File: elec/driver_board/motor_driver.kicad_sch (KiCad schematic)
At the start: 4 parts, among them IC9 TPIC6C595DG4, J9 Connector to the motor board

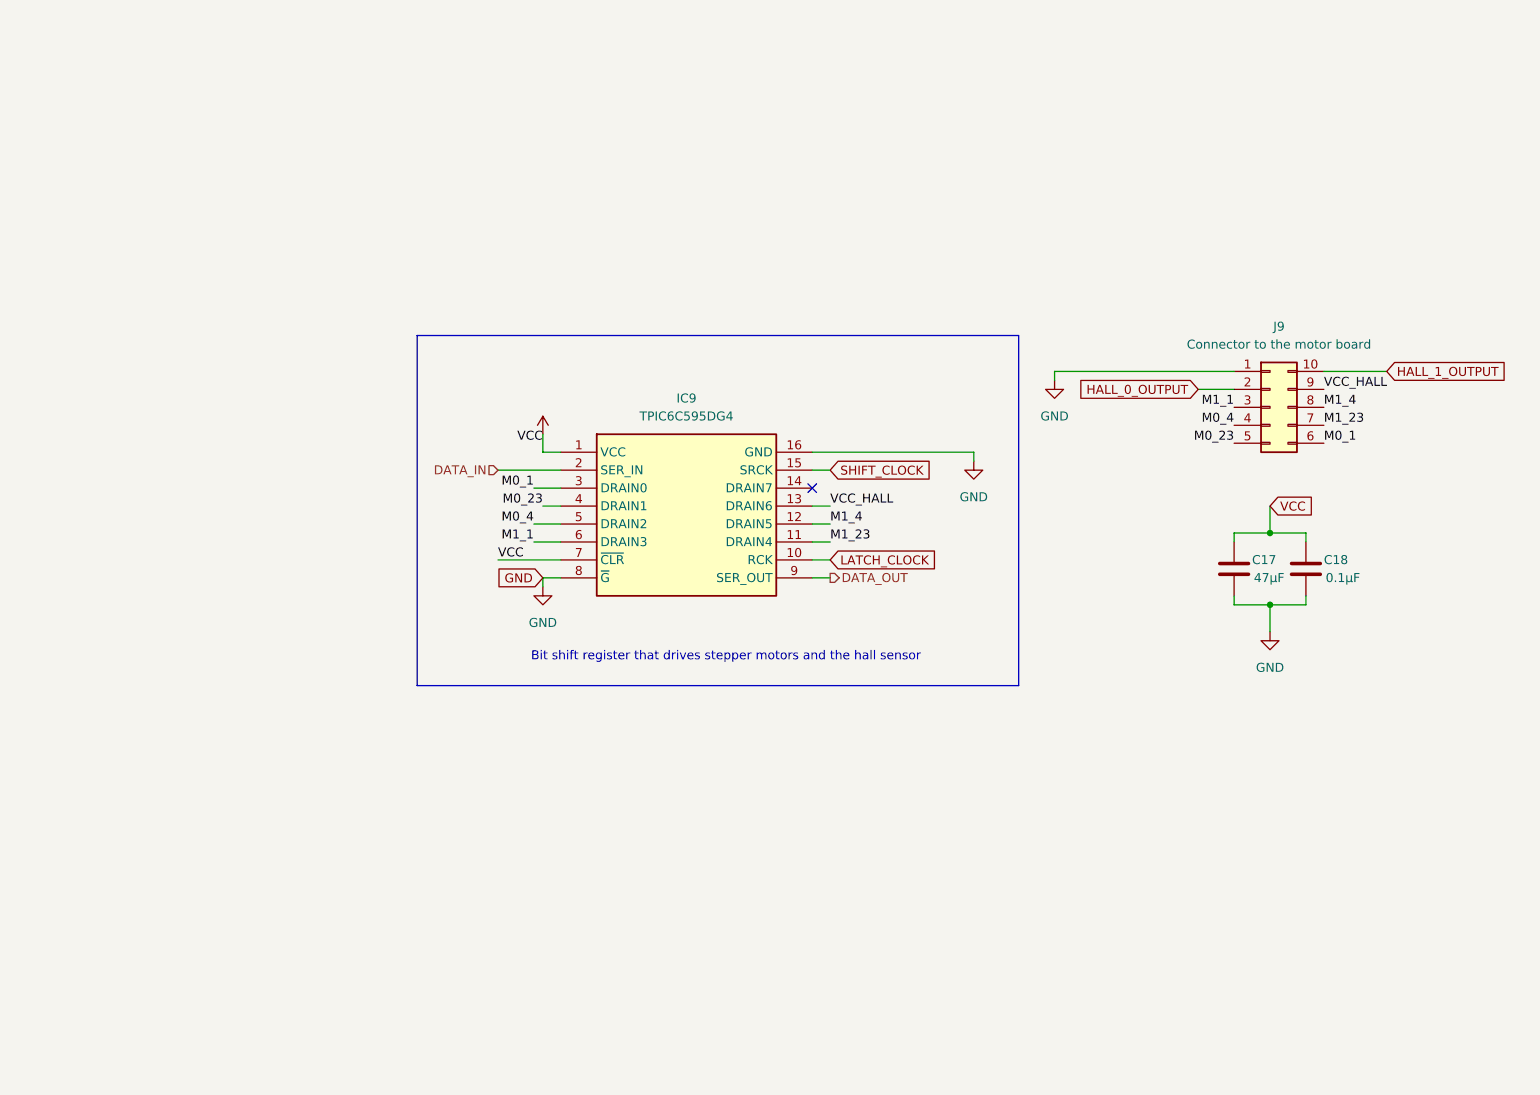
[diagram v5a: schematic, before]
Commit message: Update schematic with VID6606
Use the 'official' driver of VID28-05 motors.
Put back the 74HCT595 bit shift register to link all
motor drivers.
Work in progress.
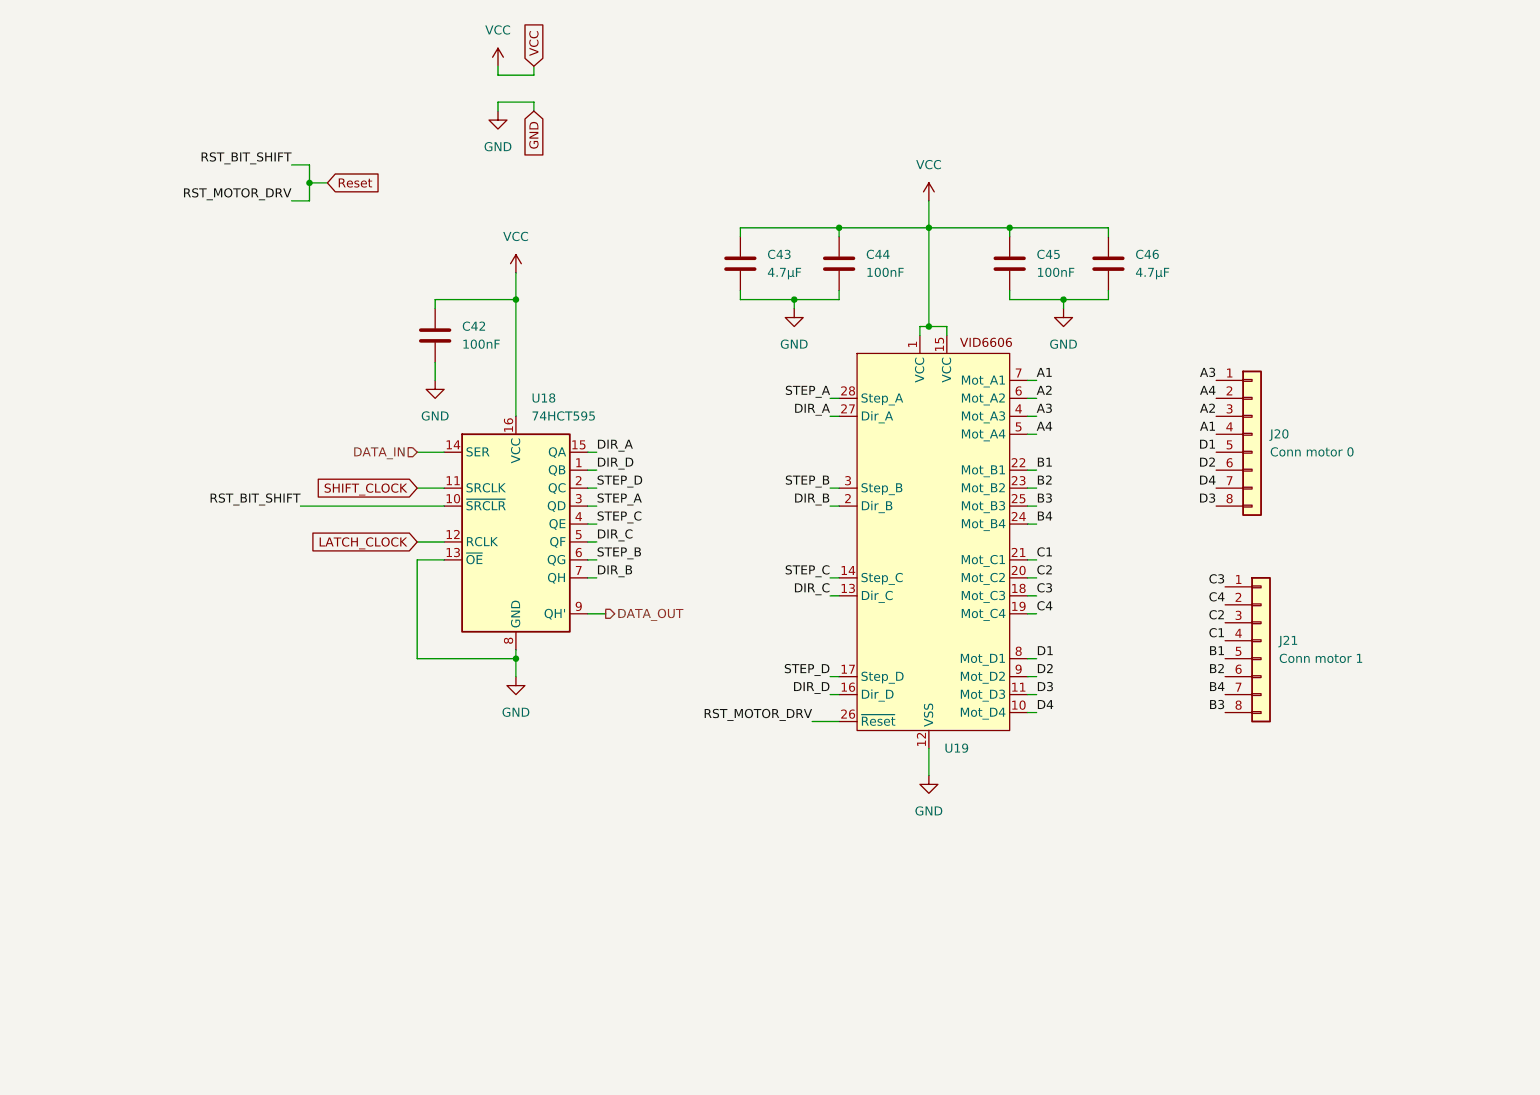
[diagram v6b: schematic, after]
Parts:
- removed C17: 47µF, Capacitor_SMD:C_1210_3225Metric_Pad1.33x2.70mm_HandSolder, symbol Device:C
- removed C18: 0.1µF, Capacitor_SMD:C_1210_3225Metric_Pad1.33x2.70mm_HandSolder, symbol Device:C
- removed IC9: TPIC6C595DG4, Samacsys:SOIC127P600X175-16N, symbol Samacsys:TPIC6C595DG4
- removed J9: Connector to the motor board, Connector_JST:JST_PH_B10B-PH-K_1x10_P2.00mm_Vertical, symbol Connector_Generic:Conn_02x05_Counter_Clockwise
- added C42, C44, C45: 100nF, Capacitor_SMD:C_0805_2012Metric, symbol Device:C
- added C43, C46: 4.7µF, Capacitor_SMD:C_0805_2012Metric, symbol Device:C
- added J20: Conn motor 0, Connector_JST:JST_PH_B8B-PH-K_1x08_P2.00mm_Vertical, symbol Connector_Generic:Conn_01x08
- added J21: Conn motor 1, Connector_JST:JST_PH_B8B-PH-K_1x08_P2.00mm_Vertical, symbol Connector_Generic:Conn_01x08
- added U18: 74HCT595, Package_SO:SOIC-16_3.9x9.9mm_P1.27mm, symbol 74xx:74HCT595
- added U19: ~, Package_SO:SOP-28_8.4x18.16mm_P1.27mm, symbol perso:VID6606
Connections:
- net DATA_IN: now also U18.14 (SER)
- net DATA_OUT: now also U18.9 (QH')
- net GND: now also C42.2, C43.2, C44.2, C45.2, C46.2, U18.13 (~{OE}), U18.8 (GND), U19.12 (VSS)
- net LATCH_CLOCK: now also U18.12 (RCLK)
- net SHIFT_CLOCK: now also U18.11 (SRCLK)
- new net A1: J20.4 (Pin_4), U19.7 (Mot_A1)
- new net A2: J20.3 (Pin_3), U19.6 (Mot_A2)
- new net A3: J20.1 (Pin_1), U19.4 (Mot_A3)
- new net A4: J20.2 (Pin_2), U19.5 (Mot_A4)
- new net B1: J21.5 (Pin_5), U19.22 (Mot_B1)
- new net B2: J21.6 (Pin_6), U19.23 (Mot_B2)
- new net B3: J21.8 (Pin_8), U19.25 (Mot_B3)
- new net B4: J21.7 (Pin_7), U19.24 (Mot_B4)
- new net C1: J21.4 (Pin_4), U19.21 (Mot_C1)
- new net C2: J21.3 (Pin_3), U19.20 (Mot_C2)
- new net C3: J21.1 (Pin_1), U19.18 (Mot_C3)
- new net C4: J21.2 (Pin_2), U19.19 (Mot_C4)
- new net D1: J20.5 (Pin_5), U19.8 (Mot_D1)
- new net D2: J20.6 (Pin_6), U19.9 (Mot_D2)
- new net D3: J20.8 (Pin_8), U19.11 (Mot_D3)
- new net D4: J20.7 (Pin_7), U19.10 (Mot_D4)
- new net DIR_A: U18.15 (QA), U19.27 (Dir_A)
- new net DIR_B: U18.7 (QH), U19.2 (Dir_B)
- new net DIR_C: U18.5 (QF), U19.13 (Dir_C)
- new net DIR_D: U18.1 (QB), U19.16 (Dir_D)
- new net Reset: U18.10 (~{SRCLR}), U19.26 (~{Reset})
- new net STEP_A: U18.3 (QD), U19.28 (Step_A)
- new net STEP_B: U18.6 (QG), U19.3 (Step_B)
- new net STEP_C: U18.4 (QE), U19.14 (Step_C)
- new net STEP_D: U18.2 (QC), U19.17 (Step_D)
- new net VCC: C42.1, C43.1, C44.1, C45.1, C46.1, U18.16 (VCC), U19.1 (VCC), U19.15 (VCC)
- no-connect marks 1 -> 0
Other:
- note removed: "Bit shift register that drives stepper motors and the hall sensor"

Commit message: New schematic + route
The new design schematic is done.
Route is ongoing
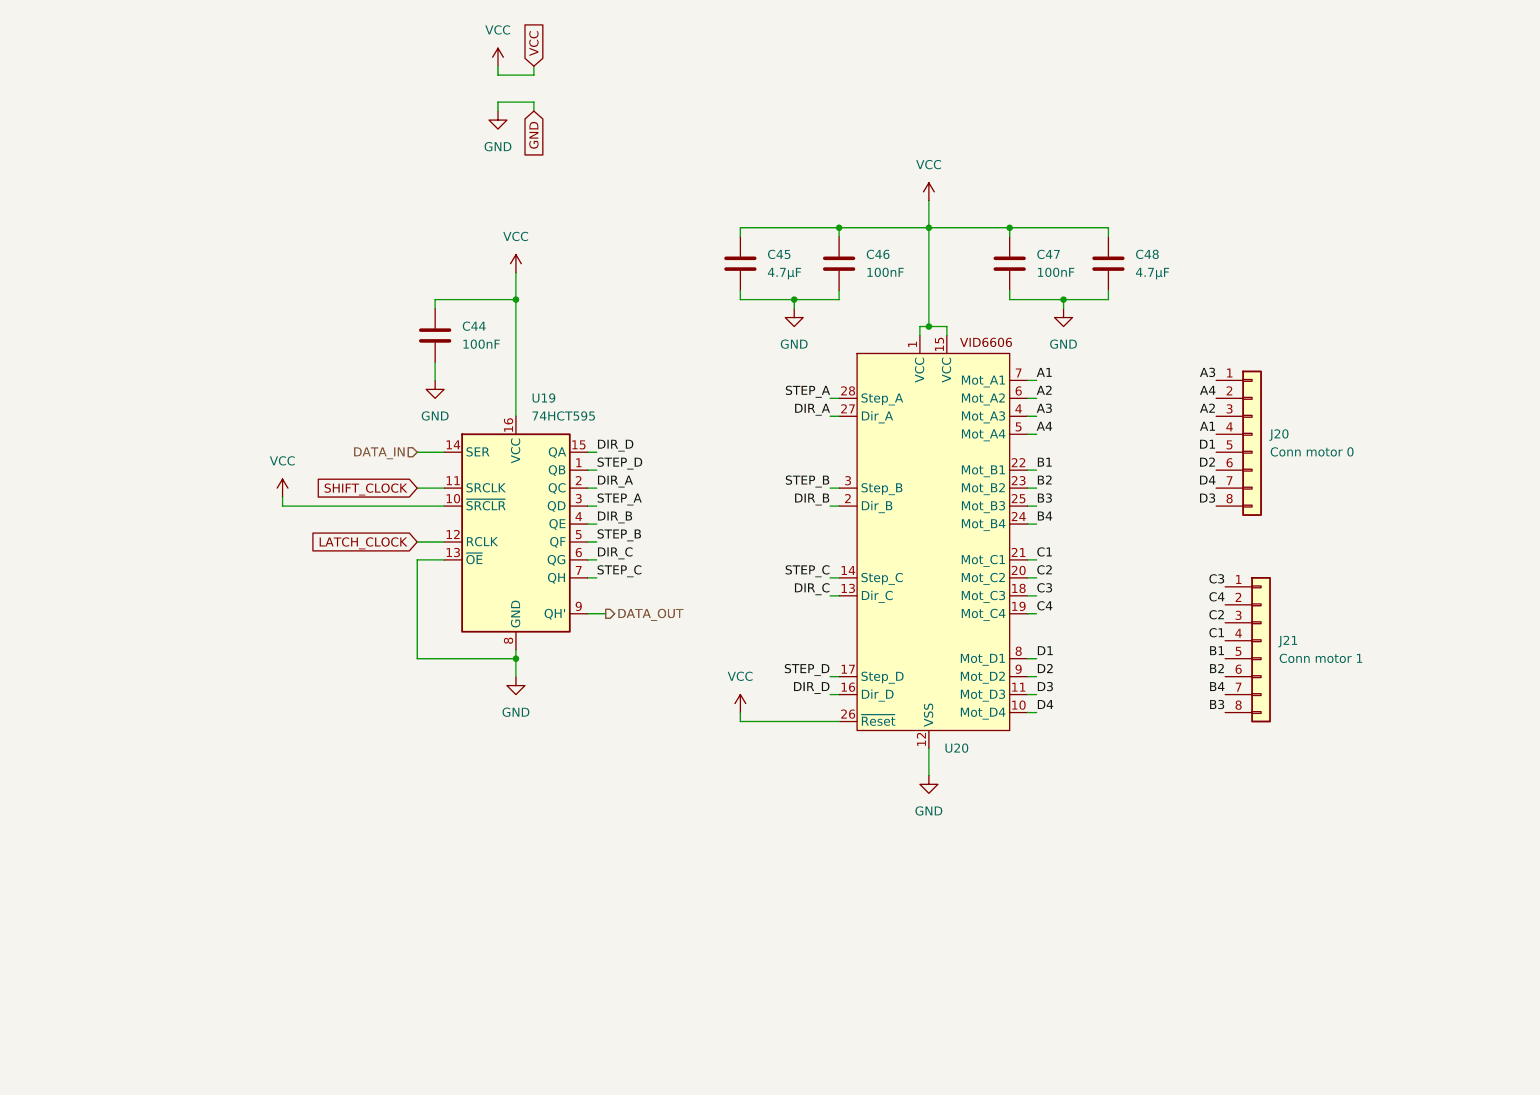
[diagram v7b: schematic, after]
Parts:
- renumbered C42 to C44, C43 to C45, C44 to C46, C45 to C47, C46 to C48, U18 to U19, U19 to U20
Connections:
- net Reset is gone; now on net VCC: U19.10 (~{SRCLR}), U20.26 (~{Reset})
- net DIR_A: now also U19.2 (QC); no longer U19.15 (QA)
- net DIR_B: now also U19.4 (QE); no longer U19.7 (QH)
- net DIR_C: now also U19.6 (QG); no longer U19.5 (QF)
- net DIR_D: now also U19.15 (QA); no longer U19.1 (QB)
- net STEP_B: now also U19.5 (QF); no longer U19.6 (QG)
- net STEP_C: now also U19.7 (QH); no longer U19.4 (QE)
- net STEP_D: now also U19.1 (QB); no longer U19.2 (QC)

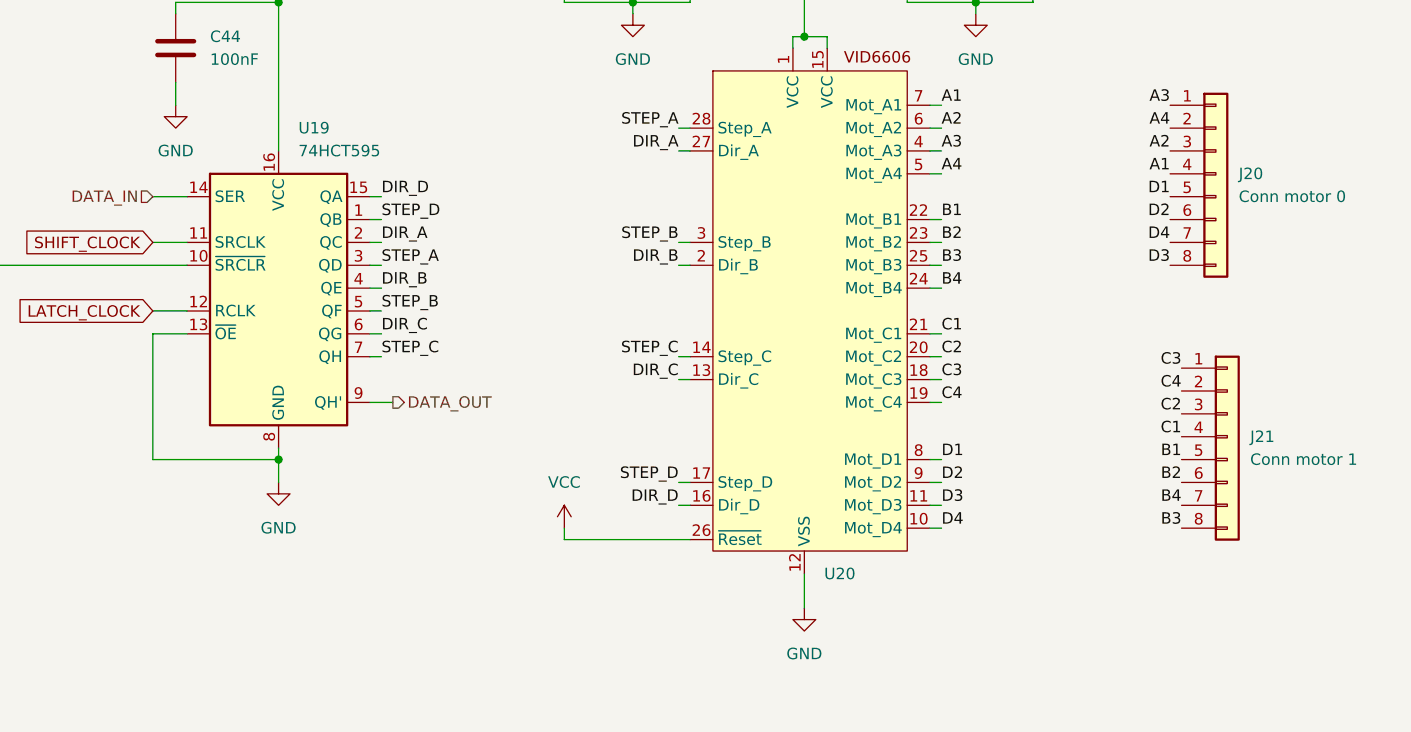
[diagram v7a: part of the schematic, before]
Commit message: PCB done, ready to be ordered
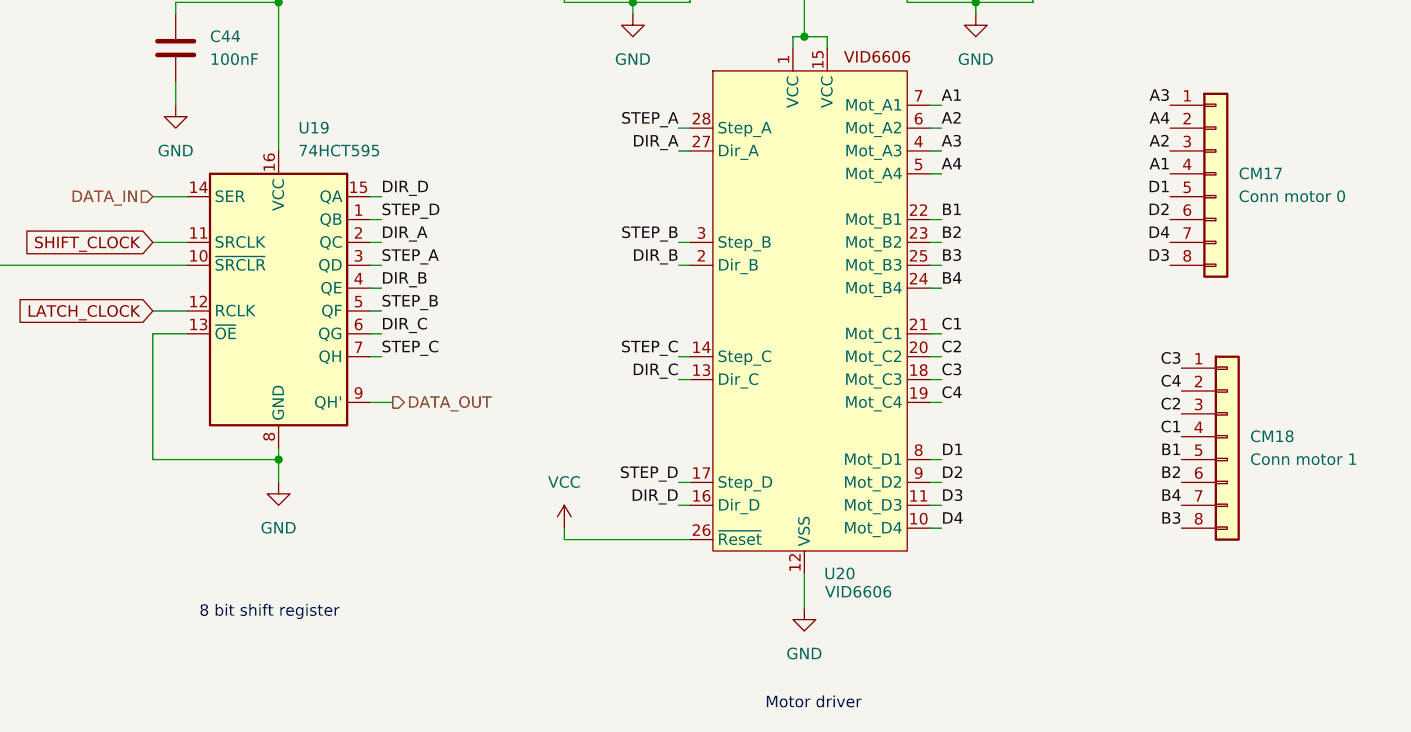
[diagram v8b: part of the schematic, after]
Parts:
- U20: value ~ -> VID6606
- renumbered J20 to CM17, J21 to CM18
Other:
- note added: "8 bit shift register"
- note added: "Motor driver"
